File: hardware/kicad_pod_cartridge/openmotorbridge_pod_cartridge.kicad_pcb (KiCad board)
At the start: 2 copper layers, 35 x 25 mm, 11 parts, among them J1 POD_BASE_SOCKET_6P, J2 JST_SH_6P_AXIAL, U1 DS2401

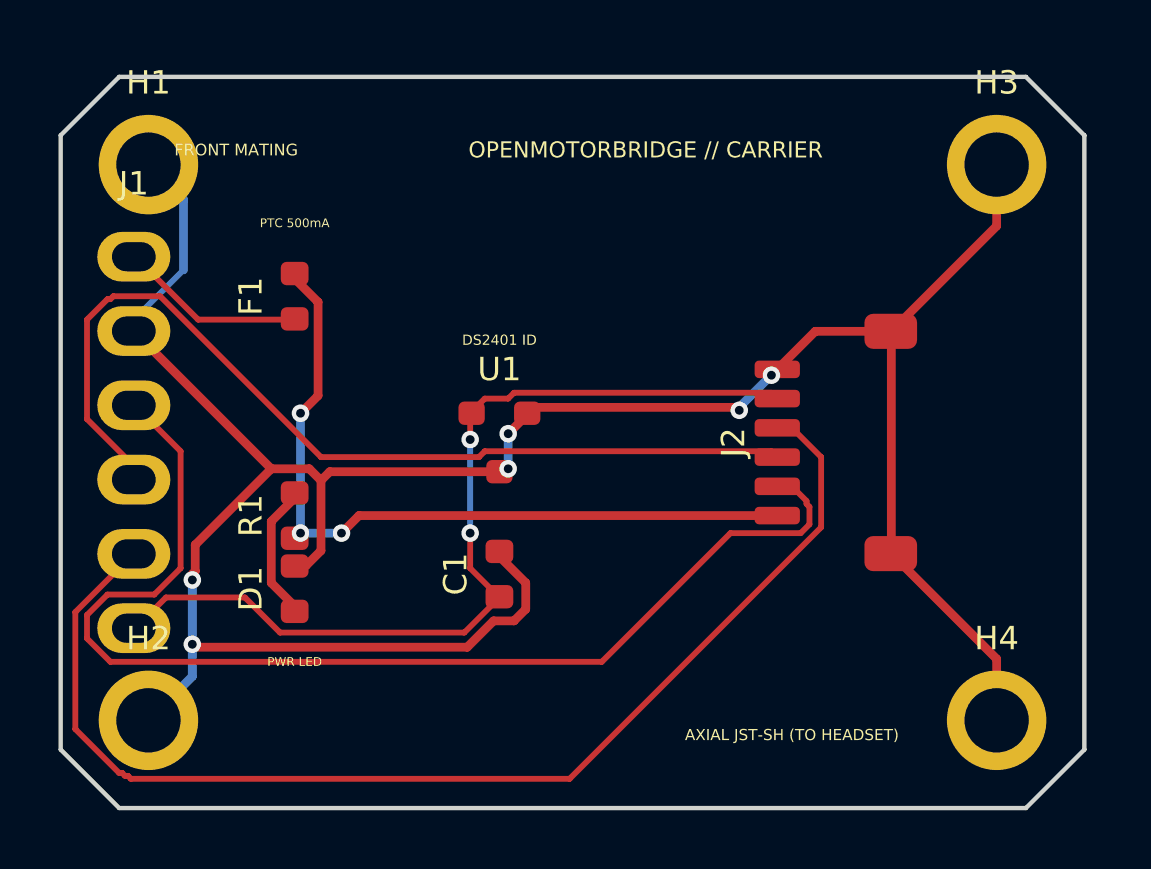
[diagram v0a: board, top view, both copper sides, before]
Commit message: feat(hardware): upgrade PCBA 03 Smart Modular Cartridge to Rev 2.0 clean canvas with CH32V003 and mechatronics
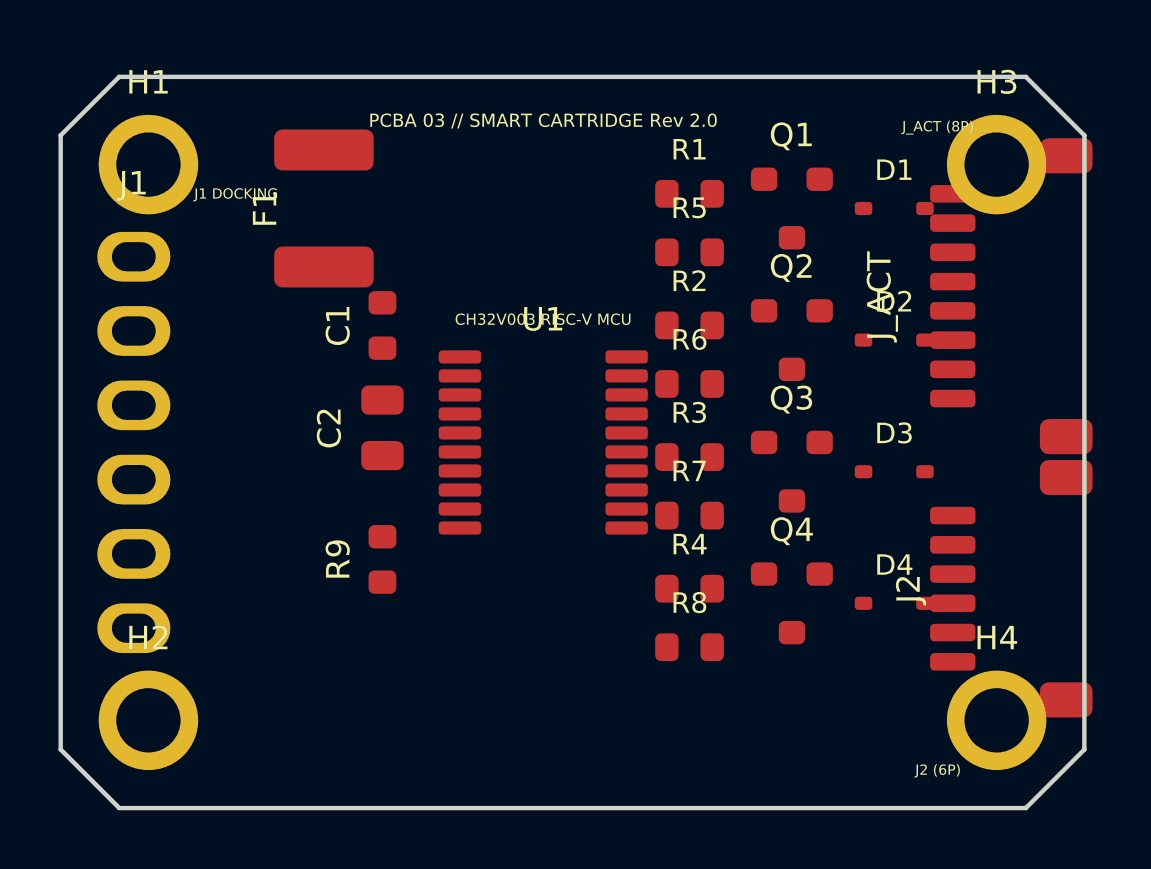
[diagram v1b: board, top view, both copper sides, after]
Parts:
- added C2: 10uF, Capacitor_SMD:C_0805_2012Metric, F.Cu at (111.0, 79.5)
- added D2: 1N4148WS, Diode_SMD:D_SOD-323, F.Cu at (128.5, 76.5)
- added D3: 1N4148WS, Diode_SMD:D_SOD-323, F.Cu at (128.5, 81.0)
- added D4: 1N4148WS, Diode_SMD:D_SOD-323, F.Cu at (128.5, 85.5)
- added J_ACT: ACTUATORS_8P, Connector_JST:JST_SH_SM08B-SRSS-TB_1x08-1MP_P1.00mm_Horizontal, F.Cu at (132.5, 75.0)
- added Q1: AO3400A, Package_TO_SOT_SMD:SOT-23, F.Cu at (125.0, 72.0)
- added Q2: AO3400A, Package_TO_SOT_SMD:SOT-23, F.Cu at (125.0, 76.5)
- added Q3: AO3400A, Package_TO_SOT_SMD:SOT-23, F.Cu at (125.0, 81.0)
- added Q4: AO3400A, Package_TO_SOT_SMD:SOT-23, F.Cu at (125.0, 85.5)
- added R2: 100R, Resistor_SMD:R_0603_1608Metric, F.Cu at (121.5, 76.0)
- added R3: 100R, Resistor_SMD:R_0603_1608Metric, F.Cu at (121.5, 80.5)
- added R4: 100R, Resistor_SMD:R_0603_1608Metric, F.Cu at (121.5, 85.0)
- added R5: 100k, Resistor_SMD:R_0603_1608Metric, F.Cu at (121.5, 73.5)
- added R6: 100k, Resistor_SMD:R_0603_1608Metric, F.Cu at (121.5, 78.0)
- added R7: 100k, Resistor_SMD:R_0603_1608Metric, F.Cu at (121.5, 82.5)
- added R8: 100k, Resistor_SMD:R_0603_1608Metric, F.Cu at (121.5, 87.0)
- added R9: 4.7k, Resistor_SMD:R_0603_1608Metric, F.Cu at (111.0, 84.0)
- D1: value GREEN_LED -> 1N4148WS; footprint LED_SMD:LED_0603_1608Metric -> Diode_SMD:D_SOD-323
- F1: value PTC_500mA -> MF-MSMF050-2; footprint Resistor_SMD:R_0603_1608Metric -> Fuse:Fuse_1812_4532Metric
- J1: value POD_BASE_SOCKET_6P -> POD_BASE_DOCKING_SOCKET_6P
- J2: value JST_SH_6P_AXIAL -> INTERCOM_HEADSET_6P
- R1: value 1.5k -> 100R
- U1: value DS2401 -> CH32V003F4P6; footprint Package_TO_SOT_SMD:SOT-23 -> Package_SO:TSSOP-20_4.4x6.5mm_P0.65mm
- moved D1 24.3 mm to (128.5, 72.0), turned to 0 degrees
- moved R1 17.4 mm to (121.5, 71.5), turned to 0 degrees
- moved C1 9.39 mm to (111.0, 76.0)
- moved J2 7.81 mm to (132.5, 85.0)
- moved F1 3.16 mm to (109.0, 72.0)
- moved U1 1.50 mm to (116.5, 80.0)
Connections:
- C1 pad 1: POD_1WIRE_ID -> VCC_5V_PROT
- D1 pad 1: NET_LED_R -> ACT_PLUS
- D1 pad 2: GND -> VCC_5V_PROT
- J1 pad 5: POD_OPTO_KEY -> POD_TRIGGER_PPS
- J1 pad 6: POD_1WIRE_ID -> POD_1WIRE
- J2 pad 2: POD_NF_P -> GND
- J2 pad 3: POD_NF_N -> POD_NF_P
- J2 pad 4: POD_OPTO_KEY -> POD_NF_N
- J2 pad 5: POD_1WIRE_ID -> MIC_IN+
- J2 pad 6: GND -> RESERVE_IO
- R1 pad 1: VCC_5V_PROT -> ACT1_GATE
- R1 pad 2: NET_LED_R -> Q1_GATE
- U1 pad 1: POD_1WIRE_ID -> (no net)
- U1 pad 2: GND -> POD_1WIRE
- U1 pad 3: GND -> POD_TRIGGER_PPS
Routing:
- net GND: track 87.5 -> 0.00 mm, vias 6 -> 0
- net POD_OPTO_KEY: track 40.9 -> 0.00 mm
- net POD_NF_P: track 40.0 -> 0.00 mm
- net POD_NF_N: track 32.0 -> 0.00 mm
- net POD_1WIRE_ID: track 31.6 -> 0.00 mm, vias 2 -> 0
- net VCC_5V_PROT: track 26.4 -> 0.00 mm, vias 3 -> 0
- net POD_VCC: track 6.44 -> 0.00 mm
- net NET_LED_R: track 4.81 -> 0.00 mm
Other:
- board text added: "CH32V003 RISC-V MCU"
- board text added: "J1 DOCKING"
- board text added: "J2 (6P)"
- board text added: "J_ACT (8P)"
- board text added: "OPENMOTORBRIDGE v8.2"
- board text added: "PCBA 03 // SMART CARTRIDGE Rev 2.0"
- board text added: "SMART MODULAR CARTRIDGE Trägerplatine (B.Cu)"
- board text removed: "AXIAL JST-SH (TO HEADSET)"
- board text removed: "DS2401 ID"
- board text removed: "FRONT MATING"
- board text removed: "OPENMOTORBRIDGE // CARRIER"
- board text removed: "OPENMOTORBRIDGE CARRIER (B.Cu)"
- board text removed: "PTC 500mA"
- board text removed: "PWR LED"

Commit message: feat(hardware): finalize manual placement, routing, 3D renders and manufacturing package for PCBA 03 Rev 2.0
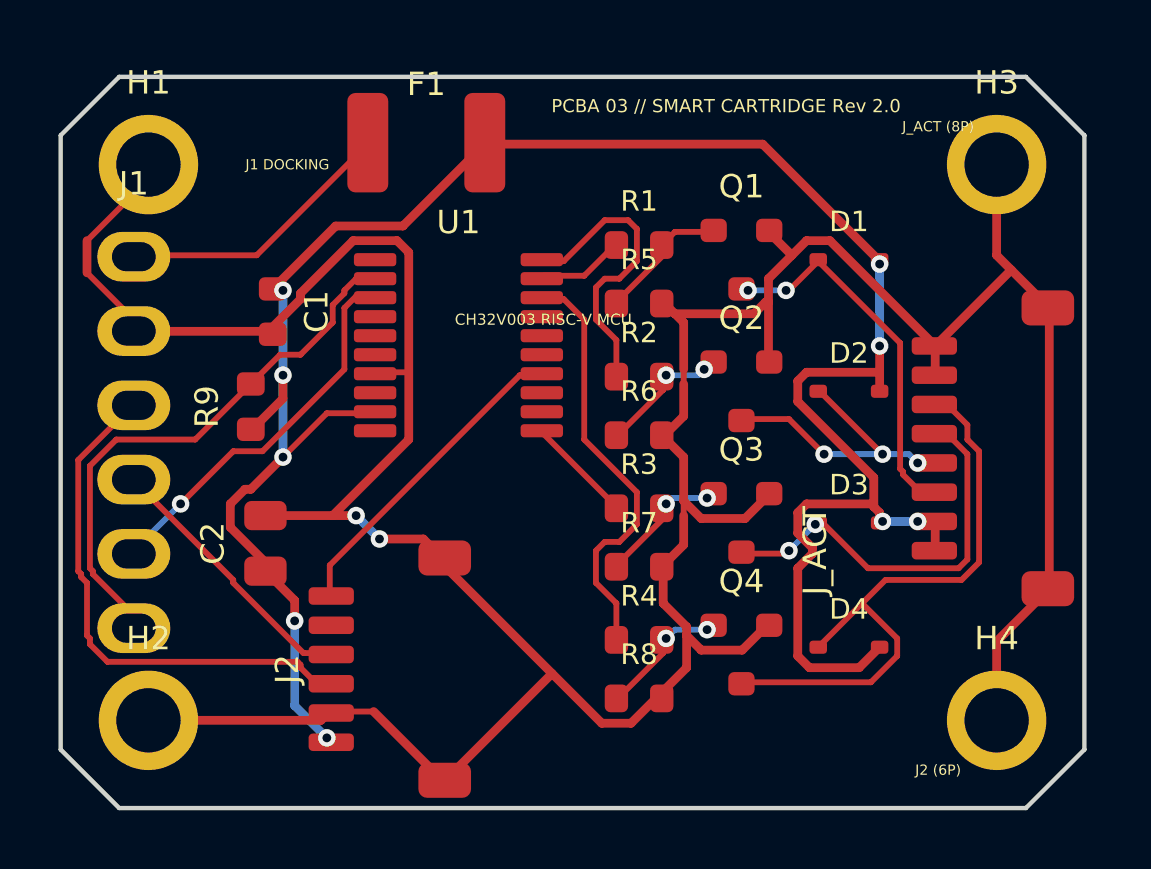
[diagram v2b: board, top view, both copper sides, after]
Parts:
- moved J2 21.4 mm to (111.2, 87.8)
- moved R9 6.90 mm to (106.5, 78.8)
- moved C2 5.62 mm to (107.0, 83.5)
- moved J_ACT 5.24 mm to (131.9, 80.2)
- moved U1 4.41 mm to (113.6, 76.7)
- moved F1 4.16 mm to (112.5, 69.8), turned to 0 degrees
- moved C1 3.78 mm to (107.2, 75.5), turned to -90 degrees
- moved Q1 2.46 mm to (123.3, 73.8)
- moved Q2 2.46 mm to (123.3, 78.2)
- moved Q3 2.46 mm to (123.3, 82.8)
- moved Q4 2.46 mm to (123.3, 87.2)
- moved R1 2.46 mm to (119.8, 73.2)
- moved R2 2.46 mm to (119.8, 77.8)
- moved R3 2.46 mm to (119.8, 82.2)
- moved R4 2.46 mm to (119.8, 86.8)
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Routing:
- net GND: track 0.00 -> 126.2 mm, vias 0 -> 2
- net VCC_5V_PROT: track 0.00 -> 76.3 mm, vias 0 -> 9
- net ACT_MESH: track 0.00 -> 21.0 mm
- net POD_1WIRE: track 0.00 -> 18.9 mm
- net POD_NF_P: track 0.00 -> 18.0 mm
- net ACT4_GATE: track 0.00 -> 14.9 mm
- net ACT_CENTER: track 0.00 -> 13.7 mm, vias 0 -> 2
- net POD_TRIGGER_PPS: track 0.00 -> 13.2 mm, vias 0 -> 1
- net ACT_PLUS: track 0.00 -> 12.9 mm, vias 0 -> 2
- net RESERVE_IO: track 0.00 -> 11.1 mm
- net ACT_MINUS: track 0.00 -> 10.5 mm, vias 0 -> 3
- net ACT2_GATE: track 0.00 -> 10.4 mm
- net POD_VCC: track 0.00 -> 9.62 mm
- net POD_NF_N: track 0.00 -> 9.27 mm
- net Q1_GATE: track 0.00 -> 4.71 mm
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
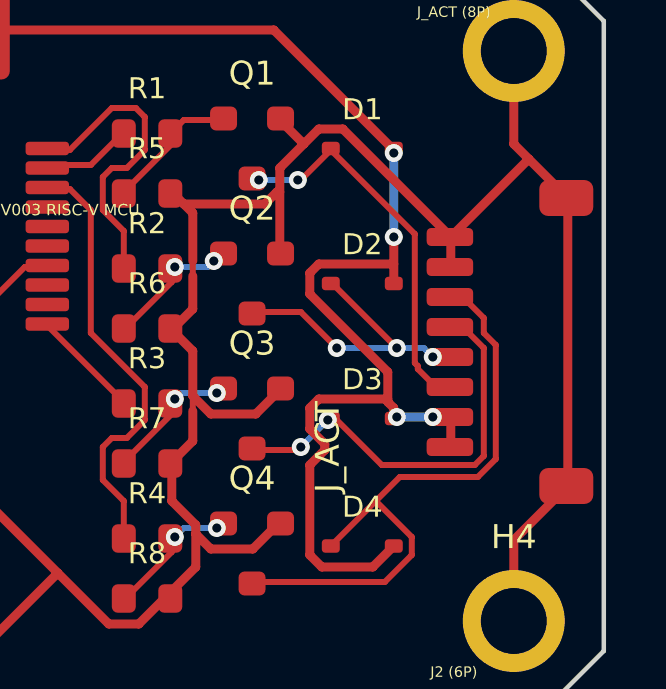
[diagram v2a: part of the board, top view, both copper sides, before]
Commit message: hardware(pcb): mathematically align edge connectors on Front Node (PCBA 05) and Pod Cartridge (PCBA 03)
- Front Node top edge: align J1, J10, J11, J2, J3, J9 to consistent Y=73.500 (fixing 50µm step) and harmonize J9-J3 clearance to 1.60 mm
- Front Node bottom edge: adjust J5 and J6 by 0.25 mm so all 6 USB/cam ports have exactly 1.600 mm clearance
- Front Node right edge: smooth J7 USB-C service port to clean 0.5 mm grid at Y=105.000
- Pod Cartridge: smooth J_ACT to X=132.000 (3.00 mm distance to edge)
- Add inspect_and_align_pcb_connectors.py diagnostic and alignment tool
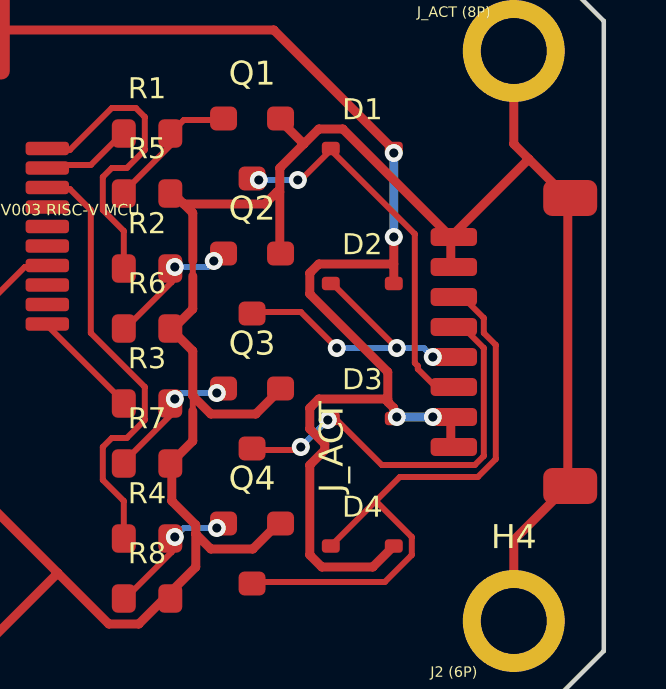
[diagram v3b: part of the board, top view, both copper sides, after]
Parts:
- moved J_ACT 0.13 mm to (132.0, 80.2)
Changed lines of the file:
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@@
 	(footprint "Connector_JST:JST_SH_SM08B-SRSS-TB_1x08-1MP_P1.00mm_Horizontal"
 		(layer "F.Cu")
-		(at 131.87 80.2 90)
+		(at 132.000 80.200 90.0)
 		(property "Reference" "J_ACT"
 			(at -3.5 -6.075 90)
